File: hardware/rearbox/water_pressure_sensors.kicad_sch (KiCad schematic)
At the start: 0 parts

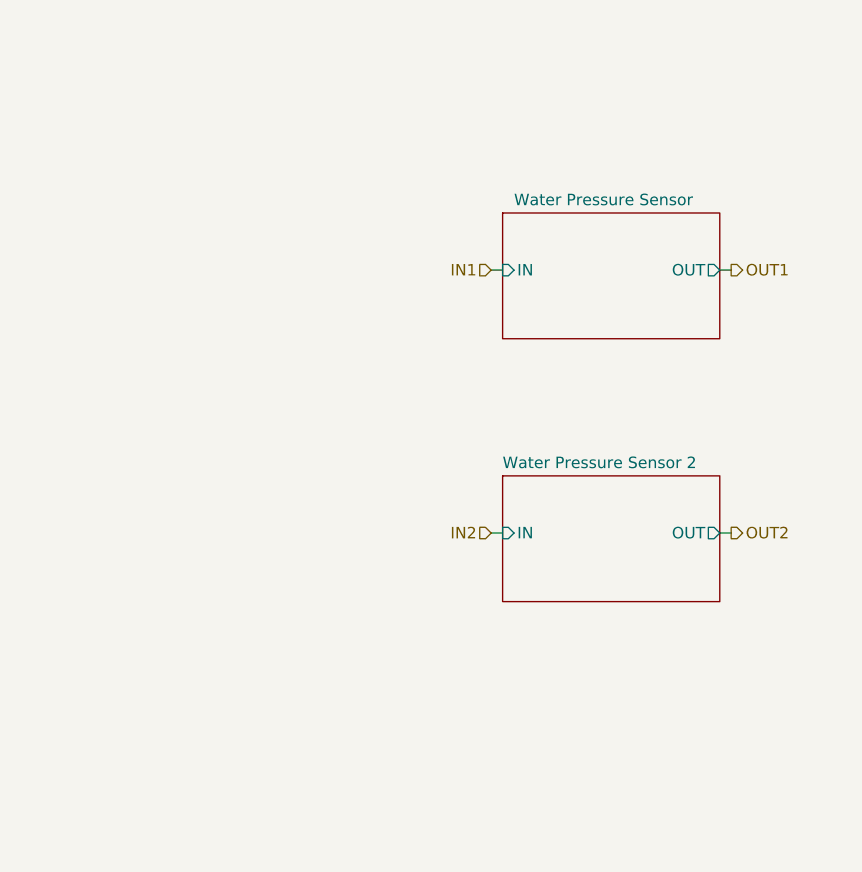
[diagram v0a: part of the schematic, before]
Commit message: Place components on the PCB
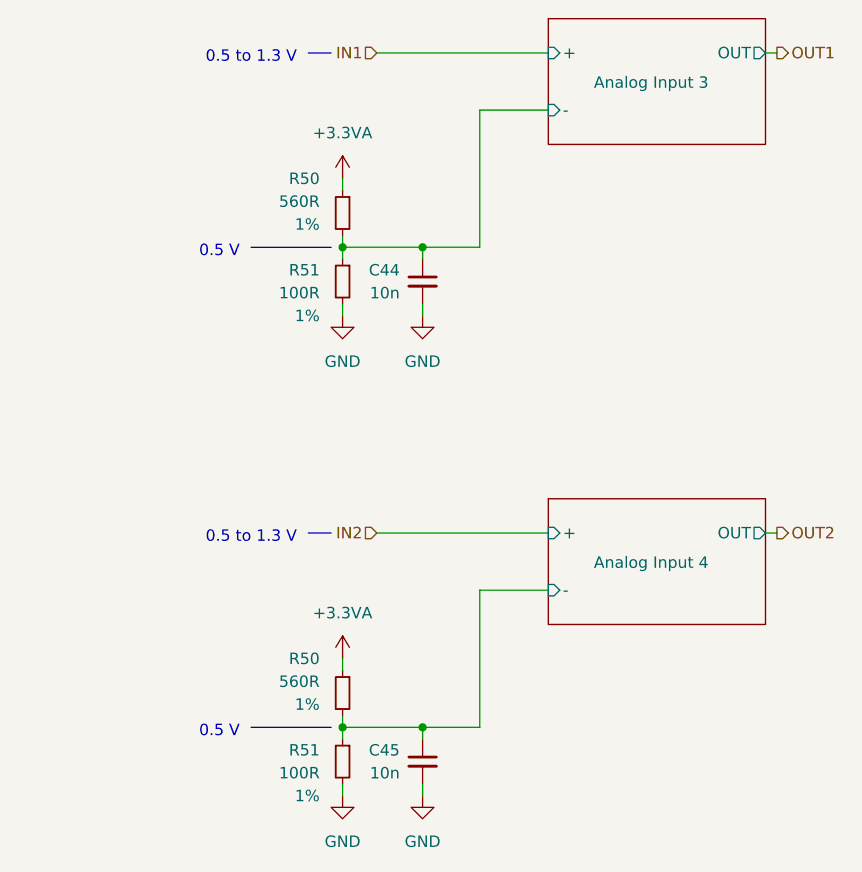
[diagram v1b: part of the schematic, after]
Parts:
- added C44, C45: 10n, Capacitor_SMD:C_0603_1608Metric, symbol Device:C_Small
- added R50 (x2): 560R, Resistor_SMD:R_0603_1608Metric, symbol Device:R_Small
- added R51 (x2): 100R, Resistor_SMD:R_0603_1608Metric, symbol Device:R_Small
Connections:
- new net +3.3VA: R50.1, R50.1
- new net Analog Input 3/-: C44.1, R50.2, R51.1
- new net Analog Input 4/-: C45.1, R50.2, R51.1
- new net GND: C44.2, C45.2, R51.2, R51.2
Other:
- removed sheet Water Pressure Sensor
- removed sheet Water Pressure Sensor 2
- added sheet Analog Input 3 (analog_input.kicad_sch)
- added sheet Analog Input 4 (analog_input.kicad_sch)
- note added: "0.5 V"
- note added: "0.5 to 1.3 V"

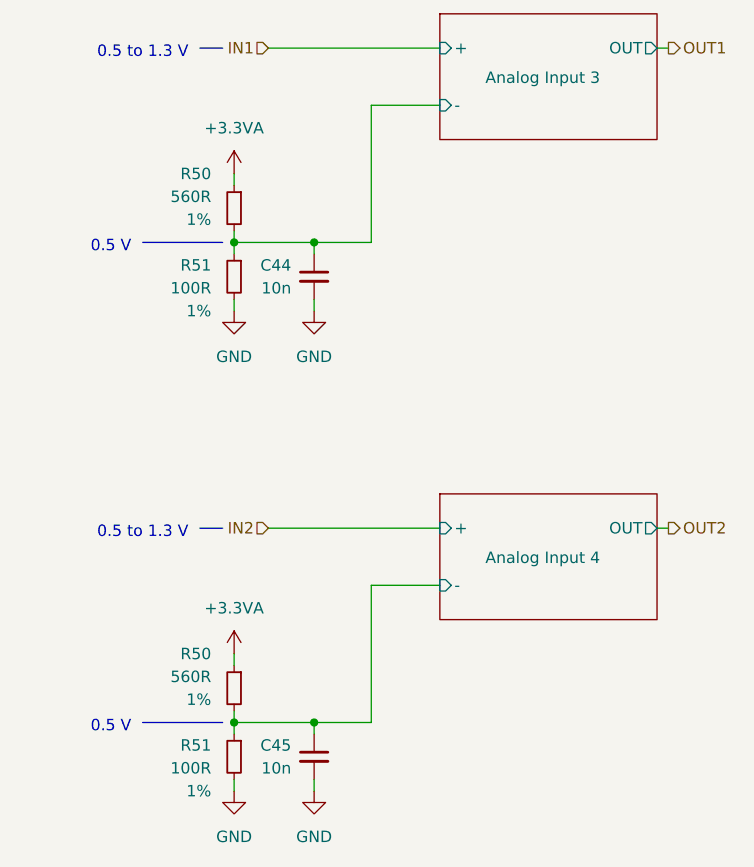
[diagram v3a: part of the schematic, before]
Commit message: Route the tracks on the connector PCB
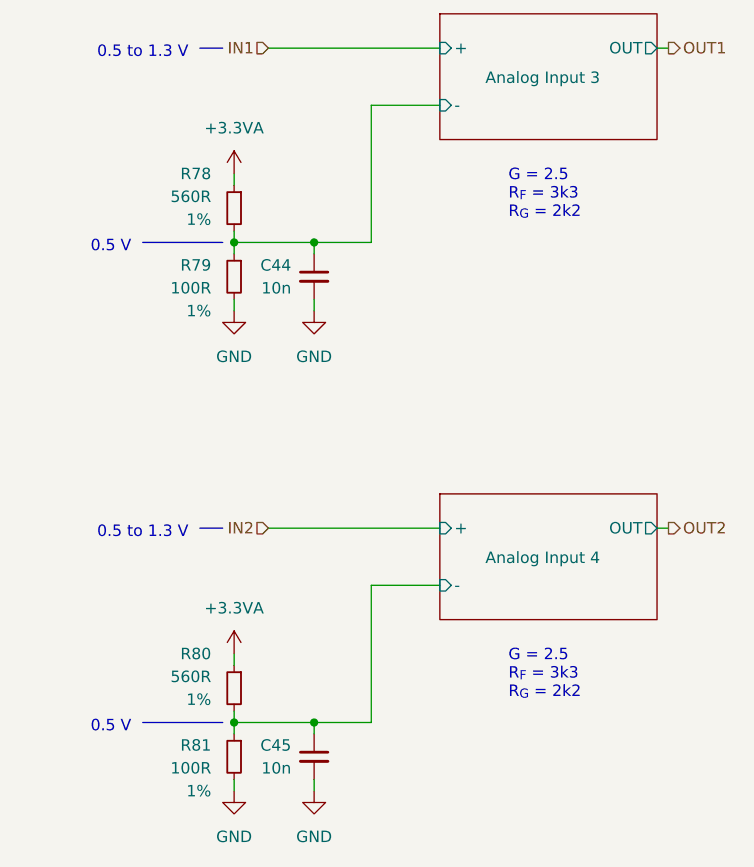
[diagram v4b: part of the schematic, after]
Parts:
- renumbered R50 to R78, R51 to R79, R50 to R80, R51 to R81
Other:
- note added: "G = 2.5 R_{F} = 3k3 R_{G} = 2k2"
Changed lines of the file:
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@@
     (effects (font (size 1.27 1.27)) (justify right bottom))
+  )
+  (text "G = 2.5\nR_{F} = 3k3\nR_{G} = 2k2" (at 207.01 73.66 0)
+    (effects (font (size 1.27 1.27)) (justify left bottom))
   )
   (text "0.5 to 1.3 V" (at 171.45 109.22 0)
     (effects (font (size 1.27 1.27)) (justify right bottom))
   )
+  (text "G = 2.5\nR_{F} = 3k3\nR_{G} = 2k2" (at 207.01 127 0)
+    (effects (font (size 1.27 1.27)) (justify left bottom))
+  )
   (hierarchical_label "IN2" (shape input) (at 180.34 107.95 180) (fields_autoplaced)
     (effects (font (size 1.27 1.27)) (justify right))
@@
   (symbol (lib_id "power:GND") (at 185.42 137.16 0) (unit 1)
     (in_bom yes) (on_board yes) (dnp no)
-    (property "Reference" "#PWR077" (at 185.42 143.51 0)
+    (property "Reference" "#PWR0169" (at 185.42 143.51 0)
       (effects (font (size 1.27 1.27)) hide)
     )
@@
     (instances
       (project "rearbox"
-        (path "/b652b05a-4e3d-4ad1-b032-18886abe7d45/264ec557-c33b-4d6e-8249-7c546f6f500a"
-          (reference "#PWR077") (unit 1)
-        )
         (path "/b652b05a-4e3d-4ad1-b032-18886abe7d45/a7dfb715-9f45-42ac-b5d4-81823a559192"
           (reference "#PWR0169") (unit 1)
@@
   (symbol (lib_id "Device:R_Small") (at 176.53 125.73 0) (mirror y) (unit 1)
     (in_bom yes) (on_board yes) (dnp no)
-    (property "Reference" "R50" (at 173.99 121.92 0)
+    (property "Reference" "R80" (at 173.99 121.92 0)
       (effects (font (size 1.27 1.27)) (justify left))
     )
@@
     (instances
       (project "rearbox"
-        (path "/b652b05a-4e3d-4ad1-b032-18886abe7d45/264ec557-c33b-4d6e-8249-7c546f6f500a"
-          (reference "R50") (unit 1)
-        )
         (path "/b652b05a-4e3d-4ad1-b032-18886abe7d45/a7dfb715-9f45-42ac-b5d4-81823a559192"
           (reference "R80") (unit 1)
@@
   (symbol (lib_id "power:GND") (at 176.53 83.82 0) (unit 1)
     (in_bom yes) (on_board yes) (dnp no)
-    (property "Reference" "#PWR077" (at 176.53 90.17 0)
+    (property "Reference" "#PWR0165" (at 176.53 90.17 0)
       (effects (font (size 1.27 1.27)) hide)
     )
@@
     (instances
       (project "rearbox"
-        (path "/b652b05a-4e3d-4ad1-b032-18886abe7d45/264ec557-c33b-4d6e-8249-7c546f6f500a"
-          (reference "#PWR077") (unit 1)
-        )
         (path "/b652b05a-4e3d-4ad1-b032-18886abe7d45/a7dfb715-9f45-42ac-b5d4-81823a559192"
           (reference "#PWR0165") (unit 1)
@@
   (symbol (lib_id "power:+3.3VA") (at 176.53 121.92 0) (unit 1)
     (in_bom yes) (on_board yes) (dnp no)
-    (property "Reference" "#PWR046" (at 176.53 125.73 0)
+    (property "Reference" "#PWR0166" (at 176.53 125.73 0)
       (effects (font (size 1.27 1.27)) hide)
     )
@@
     (instances
       (project "rearbox"
-        (path "/b652b05a-4e3d-4ad1-b032-18886abe7d45/7045152e-d7a2-42d7-9b15-138e7f2928ca"
-          (reference "#PWR046") (unit 1)
-        )
-        (path "/b652b05a-4e3d-4ad1-b032-18886abe7d45"
-          (reference "#PWR?") (unit 1)
-        )
         (path "/b652b05a-4e3d-4ad1-b032-18886abe7d45/a7dfb715-9f45-42ac-b5d4-81823a559192"
           (reference "#PWR0166") (unit 1)
@@
   (symbol (lib_id "power:GND") (at 185.42 83.82 0) (unit 1)
     (in_bom yes) (on_board yes) (dnp no)
-    (property "Reference" "#PWR077" (at 185.42 90.17 0)
+    (property "Reference" "#PWR0168" (at 185.42 90.17 0)
       (effects (font (size 1.27 1.27)) hide)
     )
@@
     (instances
       (project "rearbox"
-        (path "/b652b05a-4e3d-4ad1-b032-18886abe7d45/264ec557-c33b-4d6e-8249-7c546f6f500a"
-          (reference "#PWR077") (unit 1)
-        )
         (path "/b652b05a-4e3d-4ad1-b032-18886abe7d45/a7dfb715-9f45-42ac-b5d4-81823a559192"
           (reference "#PWR0168") (unit 1)
@@
   (symbol (lib_id "power:GND") (at 176.53 137.16 0) (unit 1)
     (in_bom yes) (on_board yes) (dnp no)
-    (property "Reference" "#PWR077" (at 176.53 143.51 0)
+    (property "Reference" "#PWR0167" (at 176.53 143.51 0)
       (effects (font (size 1.27 1.27)) hide)
     )
@@
     (instances
       (project "rearbox"
-        (path "/b652b05a-4e3d-4ad1-b032-18886abe7d45/264ec557-c33b-4d6e-8249-7c546f6f500a"
-          (reference "#PWR077") (unit 1)
-        )
         (path "/b652b05a-4e3d-4ad1-b032-18886abe7d45/a7dfb715-9f45-42ac-b5d4-81823a559192"
           (reference "#PWR0167") (unit 1)
@@
   (symbol (lib_id "Device:R_Small") (at 176.53 80.01 0) (mirror y) (unit 1)
     (in_bom yes) (on_board yes) (dnp no)
-    (property "Reference" "R51" (at 173.99 78.74 0)
+    (property "Reference" "R79" (at 173.99 78.74 0)
       (effects (font (size 1.27 1.27)) (justify left))
     )
@@
     (instances
       (project "rearbox"
-        (path "/b652b05a-4e3d-4ad1-b032-18886abe7d45/264ec557-c33b-4d6e-8249-7c546f6f500a"
-          (reference "R51") (unit 1)
-        )
         (path "/b652b05a-4e3d-4ad1-b032-18886abe7d45/a7dfb715-9f45-42ac-b5d4-81823a559192"
           (reference "R79") (unit 1)
@@
   (symbol (lib_id "Device:R_Small") (at 176.53 72.39 0) (mirror y) (unit 1)
     (in_bom yes) (on_board yes) (dnp no)
-    (property "Reference" "R50" (at 173.99 68.58 0)
+    (property "Reference" "R78" (at 173.99 68.58 0)
       (effects (font (size 1.27 1.27)) (justify left))
     )
@@
     (instances
       (project "rearbox"
-        (path "/b652b05a-4e3d-4ad1-b032-18886abe7d45/264ec557-c33b-4d6e-8249-7c546f6f500a"
-          (reference "R50") (unit 1)
-        )
         (path "/b652b05a-4e3d-4ad1-b032-18886abe7d45/a7dfb715-9f45-42ac-b5d4-81823a559192"
           (reference "R78") (unit 1)
@@
   (symbol (lib_id "Device:R_Small") (at 176.53 133.35 0) (mirror y) (unit 1)
     (in_bom yes) (on_board yes) (dnp no)
-    (property "Reference" "R51" (at 173.99 132.08 0)
+    (property "Reference" "R81" (at 173.99 132.08 0)
       (effects (font (size 1.27 1.27)) (justify left))
     )
@@
     (instances
       (project "rearbox"
-        (path "/b652b05a-4e3d-4ad1-b032-18886abe7d45/264ec557-c33b-4d6e-8249-7c546f6f500a"
-          (reference "R51") (unit 1)
-        )
         (path "/b652b05a-4e3d-4ad1-b032-18886abe7d45/a7dfb715-9f45-42ac-b5d4-81823a559192"
           (reference "R81") (unit 1)
@@
   (symbol (lib_id "power:+3.3VA") (at 176.53 68.58 0) (unit 1)
     (in_bom yes) (on_board yes) (dnp no)
-    (property "Reference" "#PWR046" (at 176.53 72.39 0)
+    (property "Reference" "#PWR0164" (at 176.53 72.39 0)
       (effects (font (size 1.27 1.27)) hide)
     )
@@
     (instances
       (project "rearbox"
-        (path "/b652b05a-4e3d-4ad1-b032-18886abe7d45/7045152e-d7a2-42d7-9b15-138e7f2928ca"
-          (reference "#PWR046") (unit 1)
-        )
-        (path "/b652b05a-4e3d-4ad1-b032-18886abe7d45"
-          (reference "#PWR?") (unit 1)
-        )
         (path "/b652b05a-4e3d-4ad1-b032-18886abe7d45/a7dfb715-9f45-42ac-b5d4-81823a559192"
           (reference "#PWR0164") (unit 1)

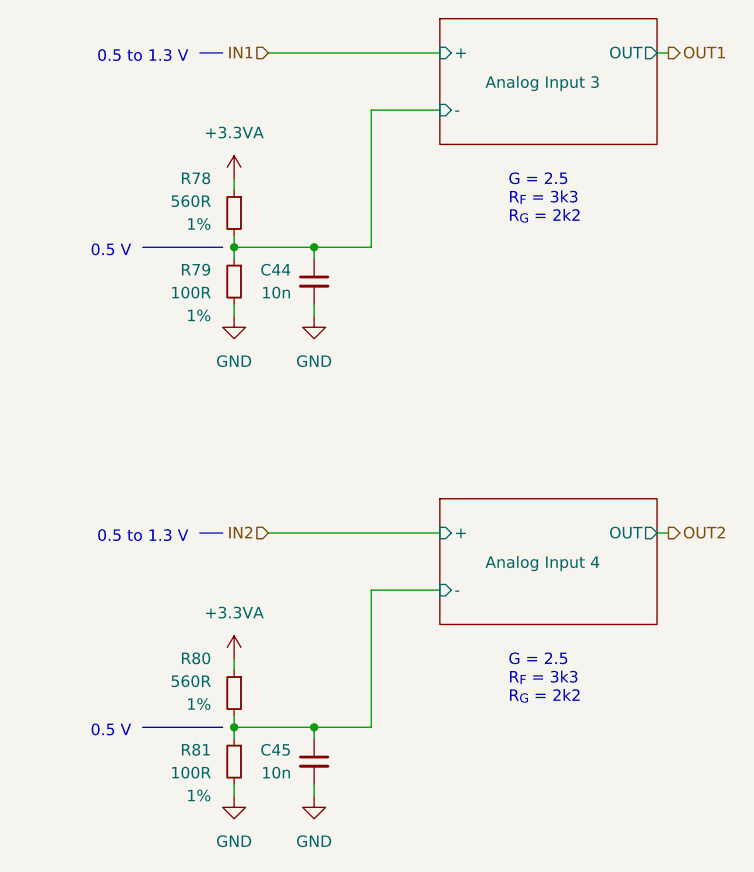
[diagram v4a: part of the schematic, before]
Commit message: Fix measurement bridges polarity
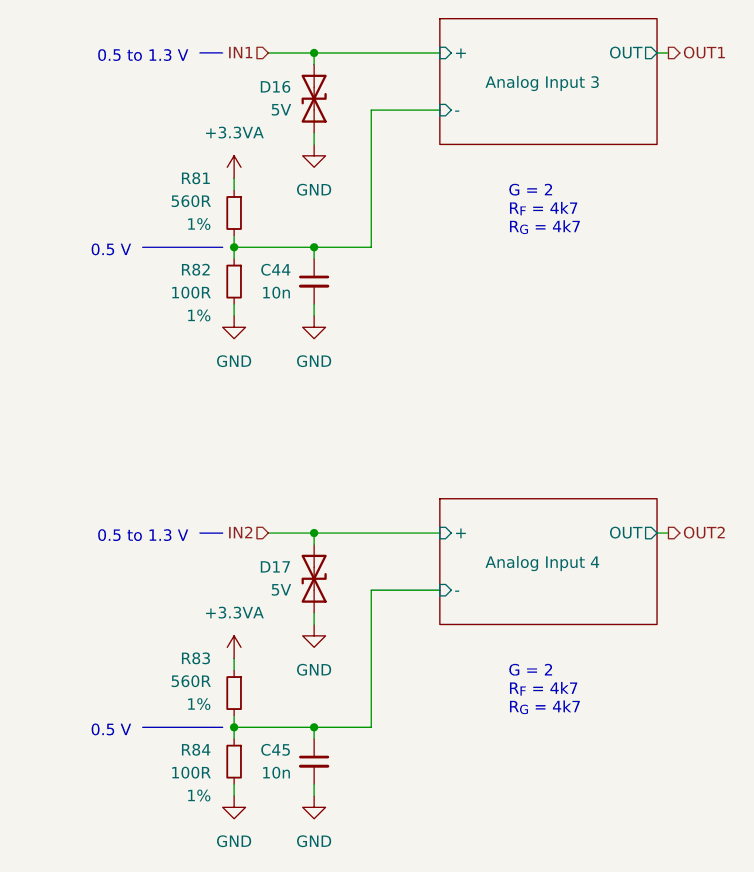
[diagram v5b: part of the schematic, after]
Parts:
- added D16, D17: 5V, Diode_SMD:D_SOD-523, symbol Device:D_TVS
- renumbered R78 to R81, R79 to R82, R80 to R83, R81 to R84
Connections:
- net GND: now also D16.1 (A1), D17.1 (A1)
- net IN1: now also D16.2 (A2)
- net IN2: now also D17.2 (A2)
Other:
- note added: "G = 2 R_{F} = 4k7 R_{G} = 4k7"
- note removed: "G = 2.5 R_{F} = 3k3 R_{G} = 2k2"
